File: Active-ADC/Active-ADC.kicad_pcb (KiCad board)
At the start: 2 copper layers, 72.6 x 55.2 mm, 18 parts, among them J1 FPGA Terminal, J2 ADC Terminal, Q1 BC847, Q2 BC847, Q3 BC847

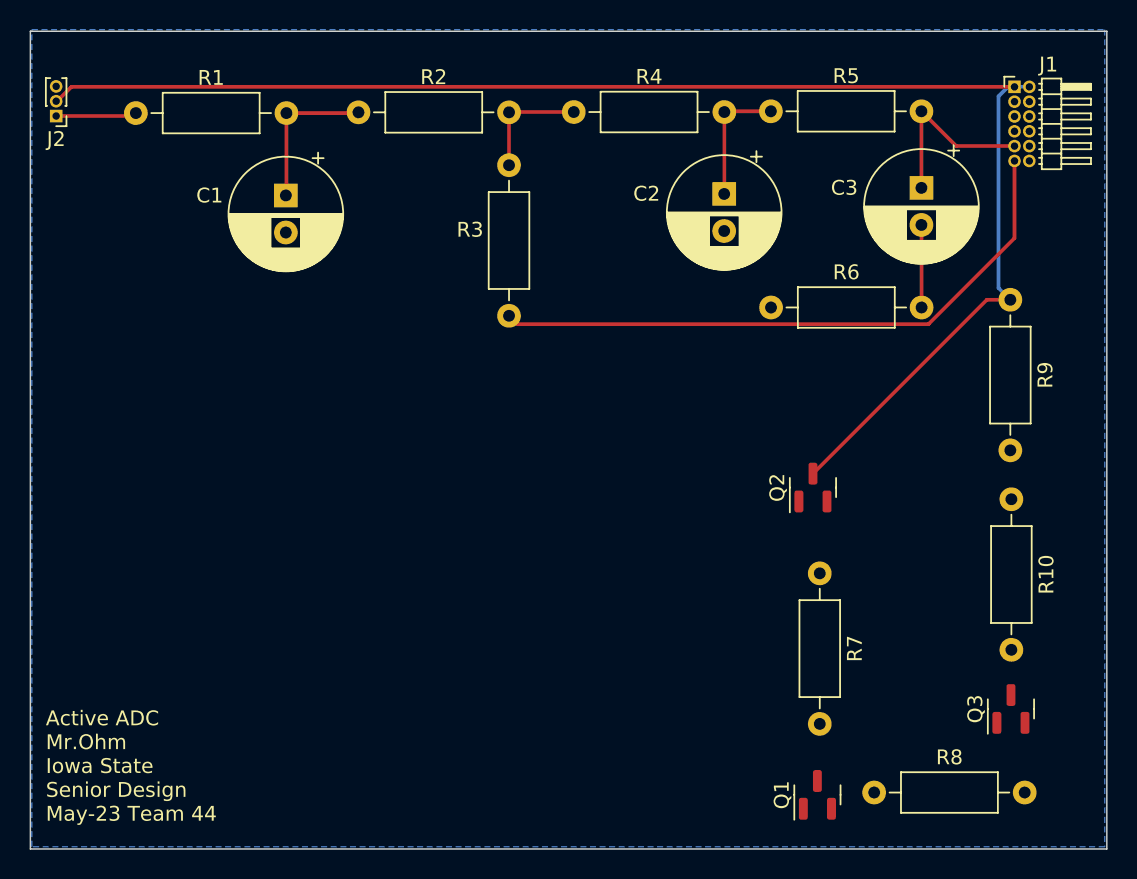
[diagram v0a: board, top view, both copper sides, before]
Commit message: Added part numbers and switched footprints to SMD
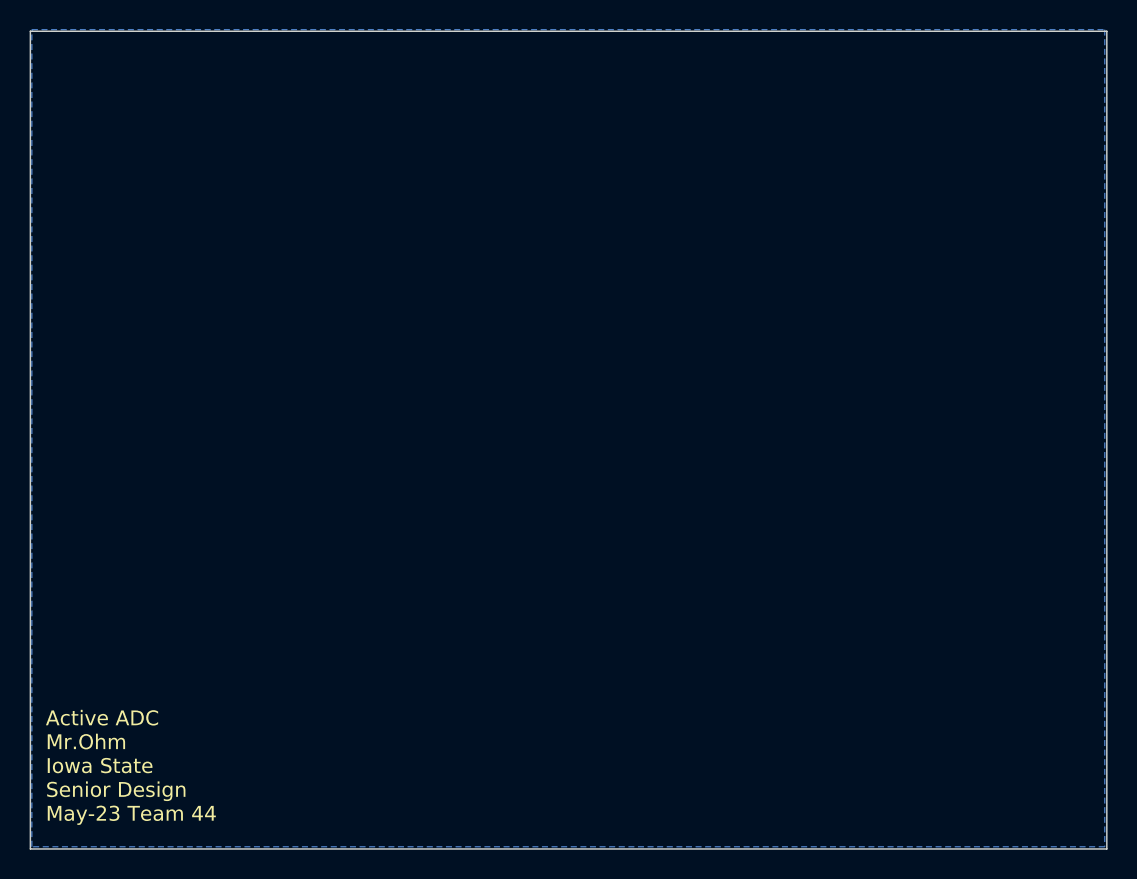
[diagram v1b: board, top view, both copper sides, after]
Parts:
- removed C1: .1u, Capacitor_THT:CP_Radial_D7.5mm_P2.50mm
- removed C2: 470p, Capacitor_THT:CP_Radial_D7.5mm_P2.50mm
- removed C3: 68p, Capacitor_THT:CP_Radial_D7.5mm_P2.50mm
- removed J1: FPGA Terminal, Connector_PinHeader_1.00mm:PinHeader_2x06_P1.00mm_Horizontal
- removed J2: ADC Terminal, Connector_PinHeader_1.00mm:PinHeader_1x03_P1.00mm_Vertical
- removed Q1, Q2, Q3: BC847, Package_TO_SOT_SMD:SOT-23
- removed R1: 100, Resistor_THT:R_Axial_DIN0207_L6.3mm_D2.5mm_P10.16mm_Horizontal
- removed R10: 2.5k, Resistor_THT:R_Axial_DIN0207_L6.3mm_D2.5mm_P10.16mm_Horizontal
- removed R2: 36k, Resistor_THT:R_Axial_DIN0207_L6.3mm_D2.5mm_P10.16mm_Horizontal
- removed R3, R4: 18k, Resistor_THT:R_Axial_DIN0207_L6.3mm_D2.5mm_P10.16mm_Horizontal
- removed R5: 56k, Resistor_THT:R_Axial_DIN0207_L6.3mm_D2.5mm_P10.16mm_Horizontal
- removed R6: 110, Resistor_THT:R_Axial_DIN0207_L6.3mm_D2.5mm_P10.16mm_Horizontal
- removed R7: 2.1k, Resistor_THT:R_Axial_DIN0207_L6.3mm_D2.5mm_P10.16mm_Horizontal
- removed R8: 375, Resistor_THT:R_Axial_DIN0207_L6.3mm_D2.5mm_P10.16mm_Horizontal
- removed R9: 1.5k, Resistor_THT:R_Axial_DIN0207_L6.3mm_D2.5mm_P10.16mm_Horizontal
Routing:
- net /3.3V: track 99.7 -> 0.00 mm
- net /FPGA-IN: track 42.0 -> 0.00 mm
- net /SIGMA-CHERRY: track 12.7 -> 0.00 mm
- net Net-(C1-Pad1): track 10.5 -> 0.00 mm
- net Net-(C2-Pad1): track 8.69 -> 0.00 mm
- net Net-(R2-Pad2): track 7.95 -> 0.00 mm
- net Net-(C3-Pad2): track 5.58 -> 0.00 mm
- net /Sensor-IN: track 5.46 -> 0.00 mm

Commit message: Updated schematic for full SMD components with part numbers
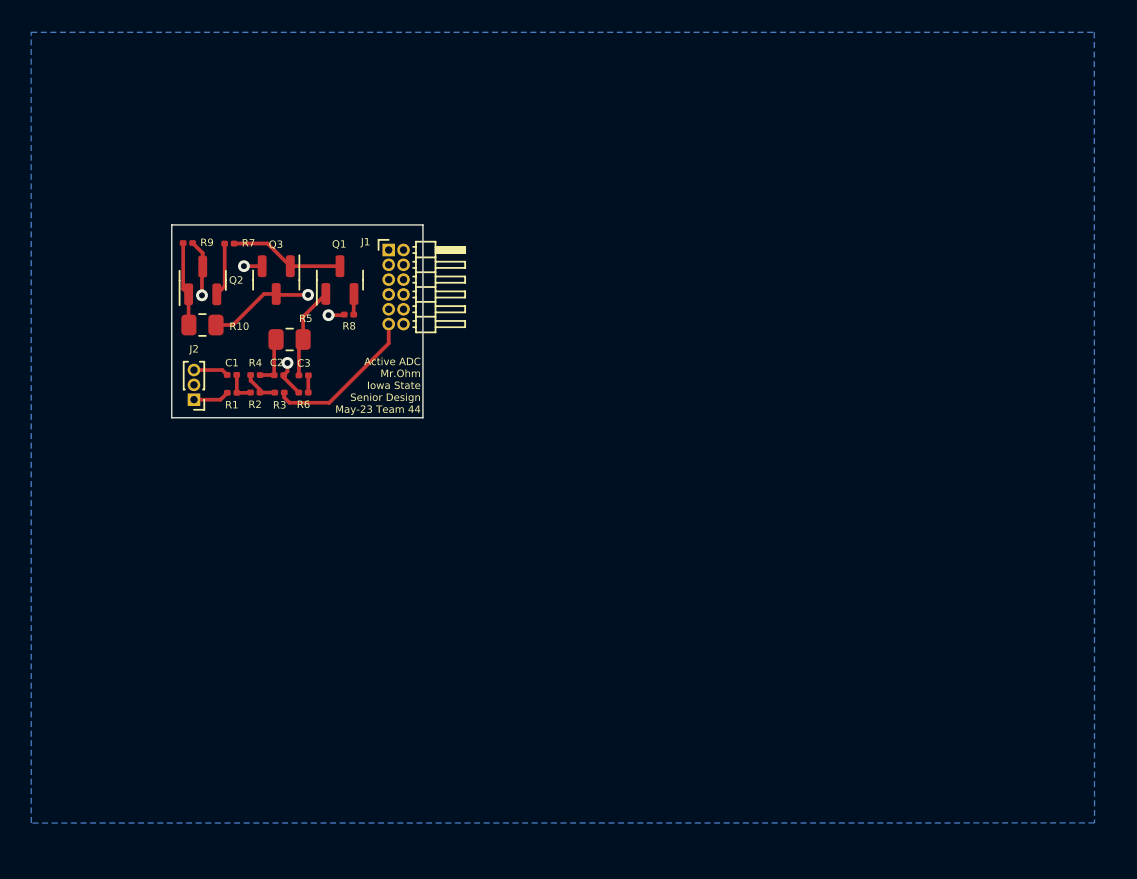
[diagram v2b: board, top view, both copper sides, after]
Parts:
- added C1: .1u, Capacitor_SMD:C_0201_0603Metric, F.Cu at (118.4, 89.0)
- added C2: 470p, Capacitor_SMD:C_0201_0603Metric, F.Cu at (121.6, 89.0)
- added C3: 68p, Capacitor_SMD:C_0201_0603Metric, F.Cu at (123.3, 89.0)
- added J1: FPGA Terminal, Connector_PinHeader_1.00mm:PinHeader_2x06_P1.00mm_Horizontal, F.Cu at (129.0, 80.6)
- added J2: ADC Terminal, Connector_PinHeader_1.00mm:PinHeader_1x03_P1.00mm_Vertical, F.Cu at (115.9, 90.7)
- added Q1: BC847, Package_TO_SOT_SMD:SOT-23, F.Cu at (125.7, 82.6)
- added Q2: BC847, Package_TO_SOT_SMD:SOT-23, F.Cu at (116.5, 82.6)
- added Q3: BC847, Package_TO_SOT_SMD:SOT-23, F.Cu at (121.4, 82.6)
- added R1: 100, Resistor_SMD:R_0201_0603Metric, F.Cu at (118.5, 90.2)
- added R10: 2.5k, Resistor_SMD:R_0805_2012Metric, F.Cu at (116.5, 85.7)
- added R2: 18k, Resistor_SMD:R_0201_0603Metric, F.Cu at (120.0, 90.2)
- added R3: 15k, Resistor_SMD:R_0201_0603Metric, F.Cu at (121.7, 90.2)
- added R4: 15k, Resistor_SMD:R_0201_0603Metric, F.Cu at (120.0, 89.0)
- added R5: 8k, Resistor_SMD:R_0805_2012Metric, F.Cu at (122.3, 86.6)
- added R6: 1170, Resistor_SMD:R_0201_0603Metric, F.Cu at (123.3, 90.2)
- added R7: 2.1k, Resistor_SMD:R_0201_0603Metric, F.Cu at (118.3, 80.2)
- added R8: 330, Resistor_SMD:R_0201_0603Metric, F.Cu at (126.3, 85.0)
- added R9: 1.5k, Resistor_SMD:R_0201_0603Metric, F.Cu at (115.5, 80.1)
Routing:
- net /FPGA-OUT: track 0.00 -> 14.5 mm, vias 0 -> 1
- net /FPGA-IN: track 0.00 -> 10.5 mm
- net Net-(Q1-Pad3): track 0.00 -> 7.78 mm
- net GND: track 0.00 -> 7.22 mm, vias 0 -> 3
- net /SIGMA-CHERRY: track 0.00 -> 6.25 mm
- net Net-(Q2-Pad1): track 0.00 -> 5.69 mm
- net /3.3V: track 0.00 -> 3.83 mm, vias 0 -> 1
- net Net-(Q2-Pad2): track 0.00 -> 3.64 mm
- net Net-(C2-Pad1): track 0.00 -> 3.42 mm
- net Net-(R2-Pad2): track 0.00 -> 2.46 mm
- net /Sensor-IN: track 0.00 -> 2.44 mm
- net Net-(C1-Pad1): track 0.00 -> 2.11 mm
- net Net-(Q1-Pad2): track 0.00 -> 1.40 mm
- net Net-(C3-Pad2): track 0.00 -> 1.16 mm
- added copper zone on In1.Cu, net /3.3V
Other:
- board size 72.6 x 55.2 mm -> 17 x 13 mm
- copper layers 2 -> 4
